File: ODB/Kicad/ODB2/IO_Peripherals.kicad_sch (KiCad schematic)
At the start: 0 parts

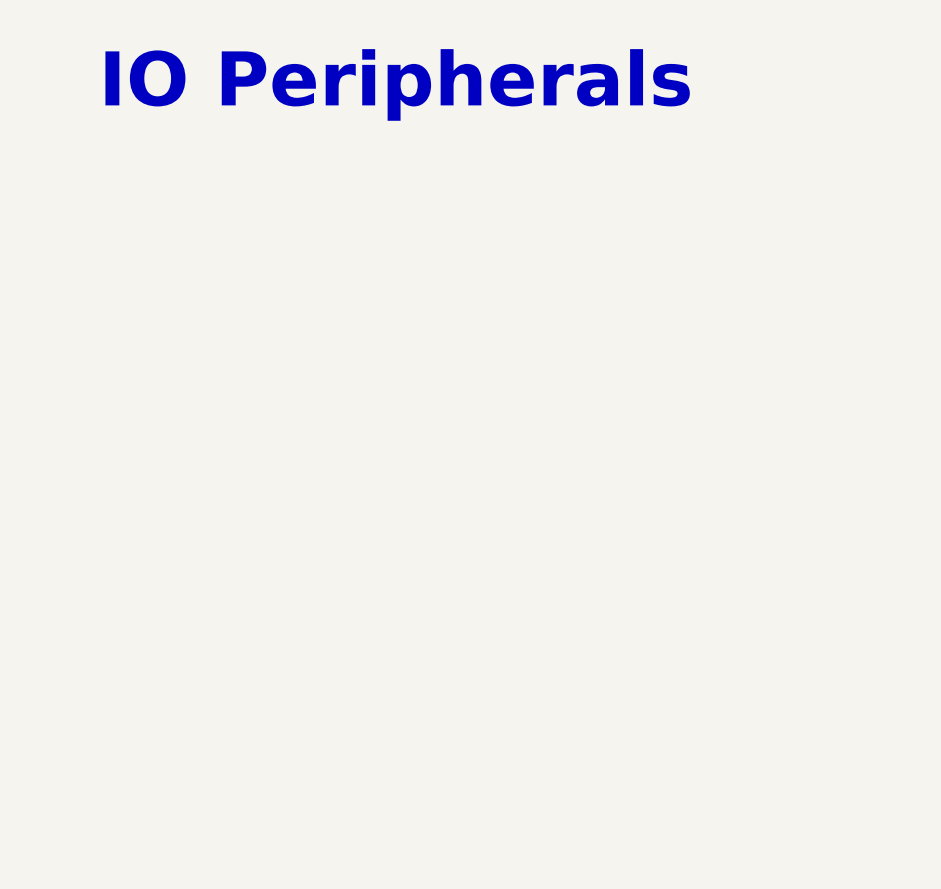
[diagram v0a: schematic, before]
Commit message: Added Usb
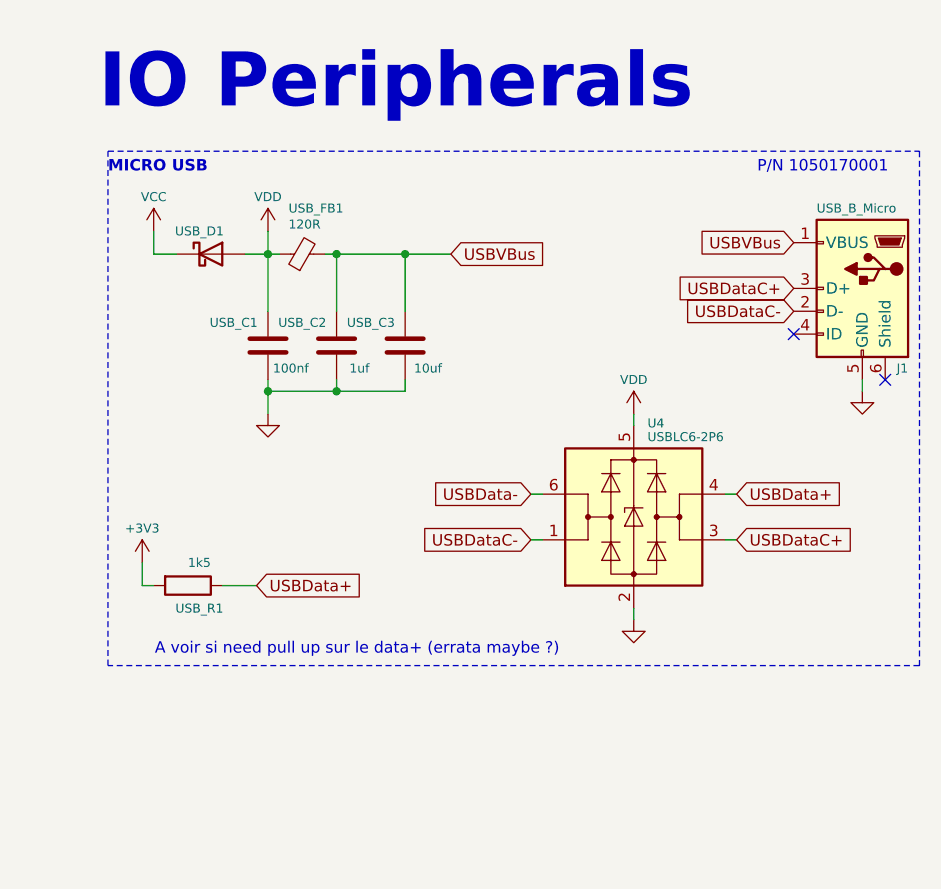
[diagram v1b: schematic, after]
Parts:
- added J1: USB_B_Micro, Connector_USB:USB_Micro-B_Molex-105017-0001, symbol Connector:USB_B_Micro
- added U4: USBLC6-2P6, Package_TO_SOT_SMD:SOT-666, symbol Power_Protection:USBLC6-2P6
- added USB_C1: 100nf, Capacitor_SMD:C_0805_2012Metric, symbol Device:C
- added USB_C2: 1uf, Capacitor_SMD:C_0805_2012Metric, symbol Device:C
- added USB_C3: 10uf, Capacitor_SMD:C_0805_2012Metric, symbol Device:C
- added USB_D1: B260A-13-F, Diode_SMD:D_SOD-123, symbol Device:D_Schottky
- added USB_FB1: 120R, Inductor_SMD:L_0805_2012Metric, symbol Device:FerriteBead_Small
- added USB_R1: 1k5, Resistor_SMD:R_0805_2012Metric, symbol Device:R
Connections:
- new net +3V3: USB_R1.2
- new net GND: J1.5 (GND), U4.2 (GND), USB_C1.1, USB_C2.1, USB_C3.1
- new net USBData+: U4.4 (I/O2), USB_R1.1
- new net USBData-: U4.6 (I/O1)
- new net USBDataC+: J1.3 (D+), U4.3 (I/O2)
- new net USBDataC-: J1.2 (D-), U4.1 (I/O1)
- new net USBVBus: J1.1 (VBUS), USB_C2.2, USB_C3.2, USB_FB1.2
- new net VCC: USB_D1.1 (K)
- new net VDD: U4.5 (VBUS), USB_C1.2, USB_D1.2 (A), USB_FB1.1
- no-connect marks 0 -> 2
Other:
- note added: "A voir si need pull up sur le data+ (errata maybe ?)"
- note added: "MICRO USB"
- note added: "P/N 1050170001"

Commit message: add SWDebug connector
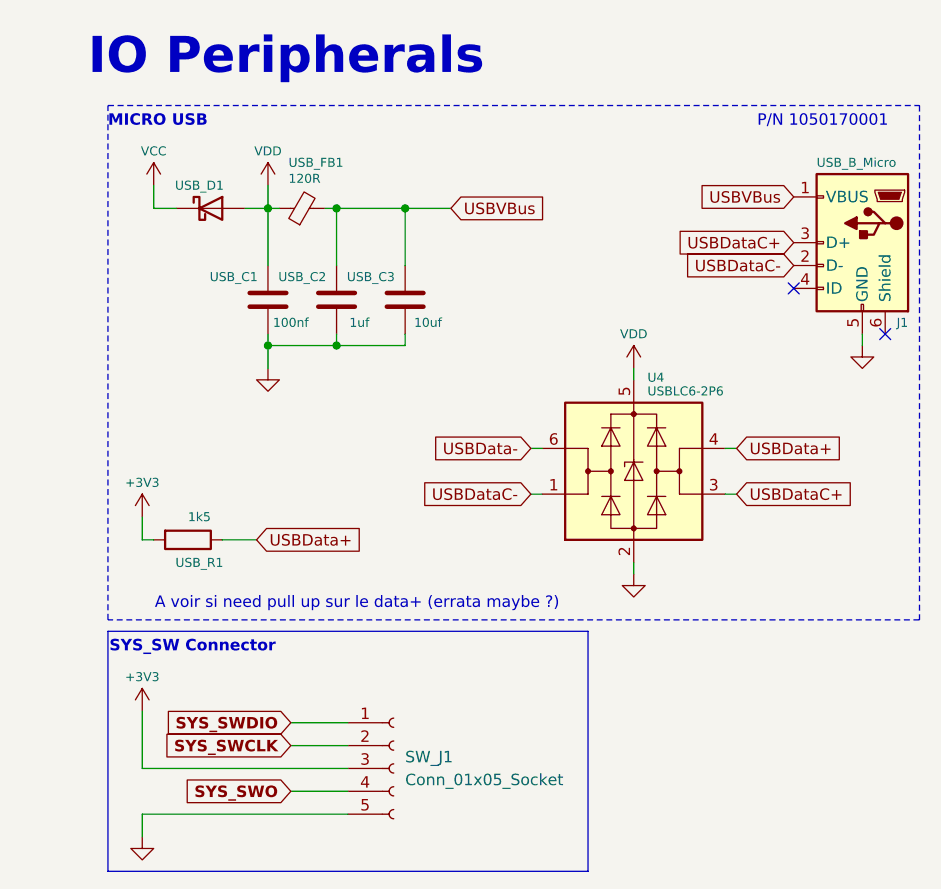
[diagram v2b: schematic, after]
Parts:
- added SW_J1: Conn_01x05_Socket, symbol Connector:Conn_01x05_Socket
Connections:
- net +3V3: now also SW_J1.3 (Pin_3)
- net GND: now also SW_J1.5 (Pin_5)
- new net SYS_SWCLK: SW_J1.2 (Pin_2)
- new net SYS_SWDIO: SW_J1.1 (Pin_1)
- new net SYS_SWO: SW_J1.4 (Pin_4)
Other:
- note added: "SYS_SW Connector"
- company: (none) -> GAUL
- title: (none) -> IO
- moved on the sheet: J1, U4, USB_C1, USB_C2, USB_C3, USB_D1, USB_FB1, USB_R1
